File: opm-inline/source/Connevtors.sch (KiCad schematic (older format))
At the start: 32 parts, among them J1 Conn_01x04_Female, J2 Conn_01x02_Female, J3 Conn_01x06_Female, J4 Conn_01x02_Female, J5 Conn_01x02_Female, U1 Metz_31349102, U2 Metz_31330102, U3 Metz_31330103, U4 Metz_31349103

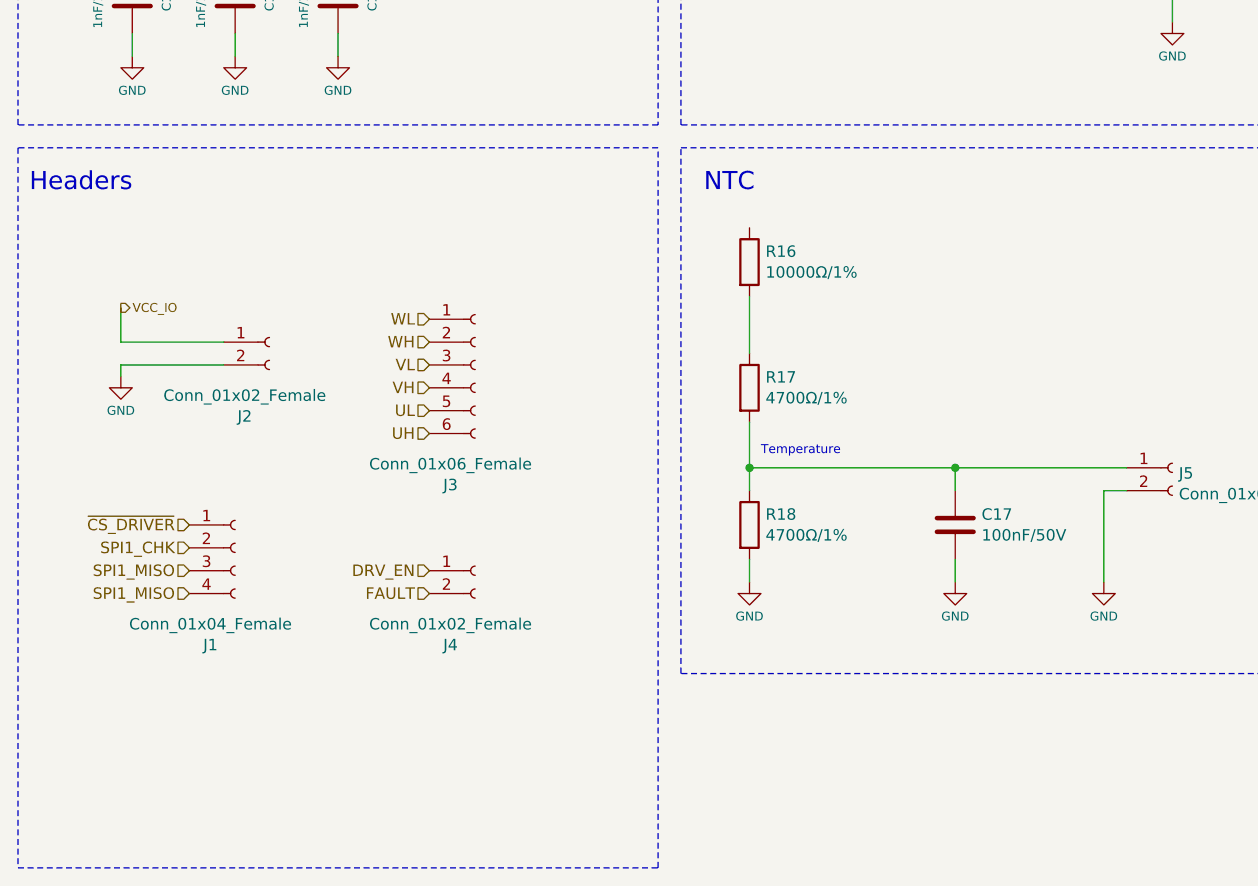
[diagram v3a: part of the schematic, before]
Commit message: adc out headers
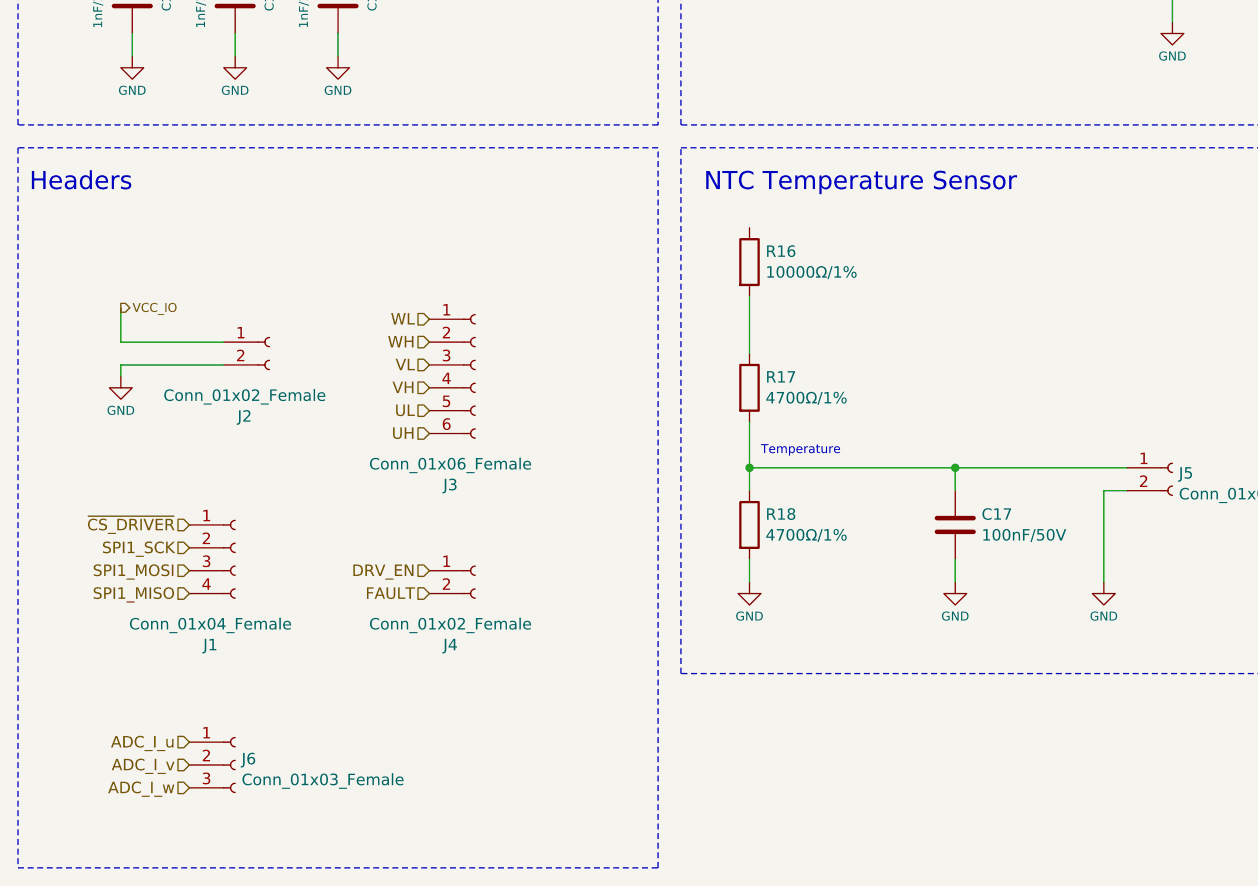
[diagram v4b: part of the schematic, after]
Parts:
- added J6: Conn_01x03_Female, Connector_PinHeader_2.54mm:PinHeader_1x03_P2.54mm_Vertical, symbol Connector:Conn_01x03_Female
- R21, R22, R23: footprint (none) -> Resistor_SMD:R_0603_1608Metric
- R24: footprint (none) -> Resistor_SMD:R_0603_1608Metric; LCSC (none) -> C23162; manf_num (none) -> 0603WAF4701T5E
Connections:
- net SPI1_MISO: no longer J1.3 (Pin_3)
- net SPI1_CHK renamed SPI1_SCK
- new net ADC_I_u: J6.1 (Pin_1)
- new net ADC_I_v: J6.2 (Pin_2)
- new net ADC_I_w: J6.3 (Pin_3)
- new net SPI1_MOSI: J1.3 (Pin_3)
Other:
- note added: "NTC Temperature Sensor"
- note removed: "NTC"
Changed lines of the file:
@@
 	3500 6050 3500 3750
 Text Notes 3600 3950 0    79   ~ 0
-NTC
+NTC Temperature Sensor
 $Comp
 L Device:R R18
@@
 FAULT
 Text HLabel 1350 5500 0    50   Input ~ 0
-SPI1_CHK
+SPI1_SCK
 Text HLabel 1350 5400 0    50   Input ~ 0
 ~CS_DRIVER
 Text HLabel 1350 5600 0    50   Input ~ 0
-SPI1_MISO
+SPI1_MOSI
 $Comp
 L Device:R R21
@@
 F 0 "R21" H 6920 3096 50  0000 L CNN
 F 1 "1000Ω/1%" H 6920 3005 50  0000 L CNN
-F 2 "" V 6780 3050 50  0001 C CNN
+F 2 "Resistor_SMD:R_0603_1608Metric" V 6780 3050 50  0001 C CNN
 F 3 "~" H 6850 3050 50  0001 C CNN
 	1    6850 3050
@@
 F 0 "R22" H 6920 3596 50  0000 L CNN
 F 1 "0Ω" H 6920 3505 50  0000 L CNN
-F 2 "" V 6780 3550 50  0001 C CNN
+F 2 "Resistor_SMD:R_0603_1608Metric" V 6780 3550 50  0001 C CNN
 F 3 "~" H 6850 3550 50  0001 C CNN
 	1    6850 3550
@@
 F 0 "R23" H 8020 3096 50  0000 L CNN
 F 1 "1500Ω/1%" H 8020 3005 50  0000 L CNN
-F 2 "" V 7880 3050 50  0001 C CNN
+F 2 "Resistor_SMD:R_0603_1608Metric" V 7880 3050 50  0001 C CNN
 F 3 "~" H 7950 3050 50  0001 C CNN
 	1    7950 3050
@@
 F 0 "R24" H 8020 3596 50  0000 L CNN
 F 1 "4700Ω/1%" H 8020 3505 50  0000 L CNN
-F 2 "" V 7880 3550 50  0001 C CNN
-F 3 "~" H 7950 3550 50  0001 C CNN
+F 2 "Resistor_SMD:R_0603_1608Metric" V 7880 3550 50  0001 C CNN
+F 3 "https://datasheet.lcsc.com/lcsc/2110252130_UNI-ROYAL-Uniroyal-Elec-0603WAF4701T5E_C23162.pdf" H 7950 3550 50  0001 C CNN
+F 4 "C23162" H 7950 3550 50  0001 C CNN "LCSC"
+F 5 "0603WAF4701T5E" H 7950 3550 50  0001 C CNN "manf_num"
 	1    7950 3550
 	1    0    0    -1
@@
 Text Notes 6900 3750 0    28   ~ 0
 Not Mounted
+$Comp
+L Connector:Conn_01x03_Female J6
+U 1 1 61C68D2F
+P 1550 6450
+F 0 "J6" H 1578 6476 50  0000 L CNN
+F 1 "Conn_01x03_Female" H 1578 6385 50  0000 L CNN
+F 2 "Connector_PinHeader_2.54mm:PinHeader_1x03_P2.54mm_Vertical" H 1550 6450 50  0001 C CNN
+F 3 "~" H 1550 6450 50  0001 C CNN
+	1    1550 6450
+	1    0    0    -1
+$EndComp
+Text HLabel 1350 6350 0    50   Input ~ 0
+ADC_I_u
+Text HLabel 1350 6450 0    50   Input ~ 0
+ADC_I_v
+Text HLabel 1350 6550 0    50   Input ~ 0
+ADC_I_w
 $EndSCHEMATC

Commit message: add pcb
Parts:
- U2: footprint TerminalBlock_MetzConnect:TerminalBlock_MetzConnect_Type011_RT05502HBWC_1x02_P5.00mm_Horizontal -> TerminalBlock:TerminalBlock_bornier-2_P5.08mm
- U3: footprint Connector_library:Metz_31330103 -> TerminalBlock:TerminalBlock_bornier-3_P5.08mm
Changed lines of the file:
@@
 F 0 "U3" H 2400 2950 39  0000 C CNN
 F 1 "Metz_31330103" H 2400 2900 39  0000 C CNN
-F 2 "Connector_library:Metz_31330103" H 2400 2350 39  0001 C CNN
+F 2 "TerminalBlock:TerminalBlock_bornier-3_P5.08mm" H 2400 2350 39  0001 C CNN
 F 3 "http://www.farnell.com/datasheets/2336348.pdf" H 2450 2650 39  0001 C CNN
 	1    2400 2700
@@
 F 0 "U2" H 1500 1100 39  0000 C CNN
 F 1 "Metz_31330102" H 1500 1150 39  0000 C CNN
-F 2 "TerminalBlock_MetzConnect:TerminalBlock_MetzConnect_Type011_RT05502HBWC_1x02_P5.00mm_Horizontal" H 1500 1150 39  0001 C CNN
+F 2 "TerminalBlock:TerminalBlock_bornier-2_P5.08mm" H 1500 1150 39  0001 C CNN
 F 3 "" H 1550 1300 39  0001 C CNN
 	1    1500 1300

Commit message: update caps
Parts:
- removed C13: 220μF/100V, Libraries:CAPE830X690N, symbol Device:CP1
- removed U1: Metz_31349102, TerminalBlock:TerminalBlock_bornier-2_P5.08mm, symbol opm-cache:Conector_library_Metz_31349102
- removed U4: Metz_31349103, TerminalBlock:TerminalBlock_bornier-3_P5.08mm, symbol opm-cache:Conector_library_Metz_31349103
- C15, C16: footprint Libraries:CAPE830X690N -> Capacitor_THT:C_Radial_D10.0mm_H20.0mm_P5.00mm; LCSC C340711 -> C338235; manf_num UCD2A221MNQ1MS -> 63ZLH330MEFC10X23
- U2: value Metz_31330102 -> TerminalBlock_2_P5.08mm
- U3: value Metz_31330103 -> TerminalBlock_3_P5.08mm
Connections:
- no-connect marks 5 -> 0
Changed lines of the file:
@@
 Text Notes 700  2450 0    79   ~ 0
 Motor Connector
-NoConn ~ 2750 2600
-NoConn ~ 2750 2700
-NoConn ~ 2750 2800
 $Comp
 L opm-cache:Conector_library_Metz_31330103 U3
@@
 P 2400 2700
 F 0 "U3" H 2400 2950 39  0000 C CNN
-F 1 "Metz_31330103" H 2400 2900 39  0000 C CNN
+F 1 "TerminalBlock_3_P5.08mm" H 2400 2900 39  0000 C CNN
 F 2 "TerminalBlock:TerminalBlock_bornier-3_P5.08mm" H 2400 2350 39  0001 C CNN
 F 3 "http://www.farnell.com/datasheets/2336348.pdf" H 2450 2650 39  0001 C CNN
@@
 	2000 3350 2000 3250
 $Comp
-L opm-cache:Conector_library_Metz_31349103 U4
-U 1 1 61BF9A89
-P 2950 2700
-F 0 "U4" V 2700 2700 39  0000 C CNN
-F 1 "Metz_31349103" V 2750 2700 39  0000 C CNN
-F 2 "TerminalBlock:TerminalBlock_bornier-3_P5.08mm" H 2925 2770 39  0001 C CNN
-F 3 "" H 2925 2770 39  0001 C CNN
-F 4 "Connected to U203" V 3150 2700 24  0000 C CNN "Info"
-	1    2950 2700
-	0    1    1    0
-$EndComp
-$Comp
 L opm-cache:Conector_library_Metz_31330102 U2
 U 1 1 61BFF192
 P 1500 1300
 F 0 "U2" H 1500 1100 39  0000 C CNN
-F 1 "Metz_31330102" H 1500 1150 39  0000 C CNN
+F 1 "TerminalBlock_2_P5.08mm" H 1500 1150 39  0000 C CNN
 F 2 "TerminalBlock:TerminalBlock_bornier-2_P5.08mm" H 1500 1150 39  0001 C CNN
 F 3 "" H 1550 1300 39  0001 C CNN
@@
 	-1   0    0    1
 $EndComp
-$Comp
-L opm-cache:Conector_library_Metz_31349102 U1
-U 1 1 61BFF3CD
-P 950 1300
-F 0 "U1" V 1150 1300 39  0000 C CNN
-F 1 "Metz_31349102" V 1100 1300 39  0000 C CNN
-F 2 "TerminalBlock:TerminalBlock_bornier-2_P5.08mm" H 950 1250 39  0001 C CNN
-F 3 "" H 950 1250 39  0001 C CNN
-F 4 "Connected to U202" V 800 1300 24  0000 C CNN "Info"
-	1    950  1300
-	0    -1   -1   0
-$EndComp
-NoConn ~ 1150 1250
-NoConn ~ 1150 1350
 Wire Wire Line
 	1700 1350 1600 1350
@@
 F 0 "C15" V 2200 1500 39  0000 C CNN
 F 1 "220μF/100V" V 2500 1500 39  0000 C CNN
-F 2 "Libraries:CAPE830X690N" V 2550 1500 39  0001 C CNN
+F 2 "Capacitor_THT:C_Radial_D10.0mm_H20.0mm_P5.00mm" V 2550 1500 39  0001 C CNN
 F 3 "~" H 2350 1500 39  0001 C CNN
-F 4 "C340711" V 2350 1500 50  0001 C CNN "LCSC"
-F 5 "UCD2A221MNQ1MS" V 2350 1500 50  0001 C CNN "manf_num"
+F 4 "C338235" V 2350 1500 50  0001 C CNN "LCSC"
+F 5 "63ZLH330MEFC10X23" V 2350 1500 50  0001 C CNN "manf_num"
 	1    2350 1500
 	1    0    0    -1
@@
 F 0 "C16" V 2700 1500 39  0000 C CNN
 F 1 "220μF/100V" V 3000 1500 39  0000 C CNN
-F 2 "Libraries:CAPE830X690N" H 2850 1500 39  0001 C CNN
+F 2 "Capacitor_THT:C_Radial_D10.0mm_H20.0mm_P5.00mm" H 2850 1500 39  0001 C CNN
 F 3 "~" H 2850 1500 39  0001 C CNN
-F 4 "C340711" V 2850 1500 50  0001 C CNN "LCSC"
-F 5 "UCD2A221MNQ1MS" V 2850 1500 50  0001 C CNN "manf_num"
+F 4 "C338235" V 2850 1500 50  0001 C CNN "LCSC"
+F 5 "63ZLH330MEFC10X23" V 2850 1500 50  0001 C CNN "manf_num"
 	1    2850 1500
 	1    0    0    -1
@@
 	2850 1250 3100 1250
 Connection ~ 2850 1250
-Wire Wire Line
-	1600 1250 1950 1250
-Wire Wire Line
-	1700 1750 1950 1750
-Wire Wire Line
-	1950 1350 1950 1250
-Connection ~ 1950 1250
-Wire Wire Line
-	1950 1250 2350 1250
-Wire Wire Line
-	1950 1650 1950 1750
-Connection ~ 1950 1750
-Wire Wire Line
-	1950 1750 2350 1750
-$Comp
-L Device:CP1 C13
-U 1 1 61C10958
-P 1950 1500
-F 0 "C13" V 1800 1500 39  0000 C CNN
-F 1 "220μF/100V" V 2100 1500 39  0000 C CNN
-F 2 "Libraries:CAPE830X690N" V 2150 1500 39  0001 C CNN
-F 3 "~" H 1950 1500 39  0001 C CNN
-F 4 "C340711" V 1950 1500 50  0001 C CNN "LCSC"
-F 5 "UCD2A221MNQ1MS" V 1950 1500 50  0001 C CNN "manf_num"
-	1    1950 1500
-	1    0    0    -1
-$EndComp
 Wire Notes Line
 	600  3750 600  6900
@@
 Text HLabel 1350 6550 0    50   Input ~ 0
 ADC_I_w
+Wire Wire Line
+	1600 1250 2350 1250
+Wire Wire Line
+	1700 1750 2350 1750
 $EndSCHEMATC

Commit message: more placements
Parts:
- C15, C16: value 220μF/100V -> 330μF/63V
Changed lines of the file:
@@
 P 2350 1500
 F 0 "C15" V 2200 1500 39  0000 C CNN
-F 1 "220μF/100V" V 2500 1500 39  0000 C CNN
+F 1 "330μF/63V" V 2500 1500 39  0000 C CNN
 F 2 "Capacitor_THT:C_Radial_D10.0mm_H20.0mm_P5.00mm" V 2550 1500 39  0001 C CNN
 F 3 "~" H 2350 1500 39  0001 C CNN
@@
 P 2850 1500
 F 0 "C16" V 2700 1500 39  0000 C CNN
-F 1 "220μF/100V" V 3000 1500 39  0000 C CNN
+F 1 "330μF/63V" V 3000 1500 39  0000 C CNN
 F 2 "Capacitor_THT:C_Radial_D10.0mm_H20.0mm_P5.00mm" H 2850 1500 39  0001 C CNN
 F 3 "~" H 2850 1500 39  0001 C CNN
